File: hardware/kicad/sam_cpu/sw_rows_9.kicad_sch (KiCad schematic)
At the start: 47 parts, among them J12 J12 SWITCH ROWS, U10 LM339, U11 LM339, U18 74HC165

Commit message: Use 3.96 mm KK-396 footprints for the switch harness connectors
J1, J2, J3, J6, J12 and J13 are 0.156" headers on the original board, so
the existing harness plugs need KK-396, as already used for J10 and J11.

Co-Authored-By: Claude Opus 5.5 (1M context) <noreply@anthropic.com>
Claude-Session: https://claude.ai/code/session_019DLTv1F2PjepjxqiUcAMKV
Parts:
- J12: footprint Connector_Molex:Molex_KK-254_AE-6410-10A_1x10_P2.54mm_Vertical -> Connector_Molex:Molex_KK-396_A-41791-0010_1x10_P3.96mm_Vertical
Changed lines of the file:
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@@
 			)
 		)
-		(property "Footprint" "Connector_Molex:Molex_KK-254_AE-6410-10A_1x10_P2.54mm_Vertical"
+		(property "Footprint" "Connector_Molex:Molex_KK-396_A-41791-0010_1x10_P3.96mm_Vertical"
 			(at 20.32 147.32 0)
 			(hide yes)

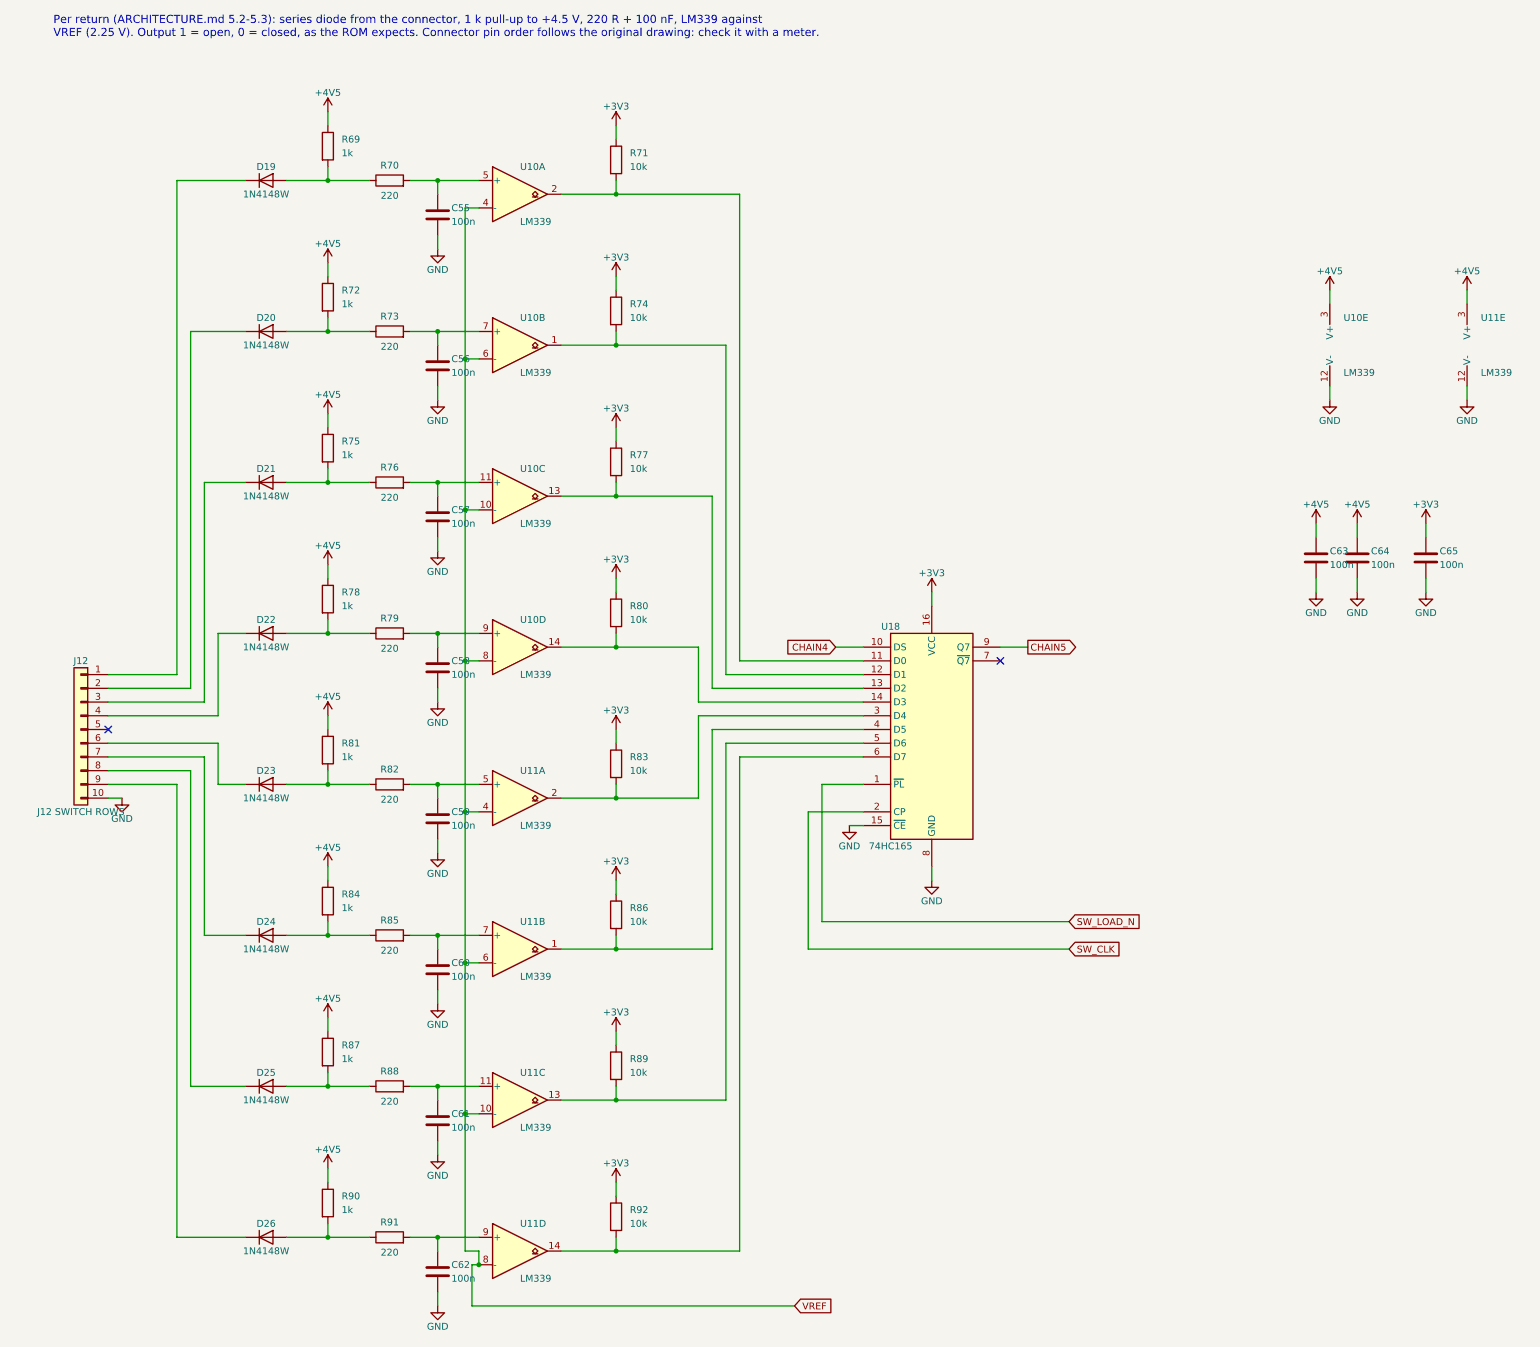
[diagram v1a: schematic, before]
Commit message: DIP switch block not loaded; larger schematic text
c30: SW3, R168-R175, U14 and C93 flagged DNP (schematic and board).
c31: schematic text 1.27 -> 1.6 mm (pins 1.5 mm), intersheet refs moved out.

Co-Authored-By: Claude Opus 5.5 (1M context) <noreply@anthropic.com>
Claude-Session: https://claude.ai/code/session_01ExuDVoDDDHhVWjb8EwVzYb
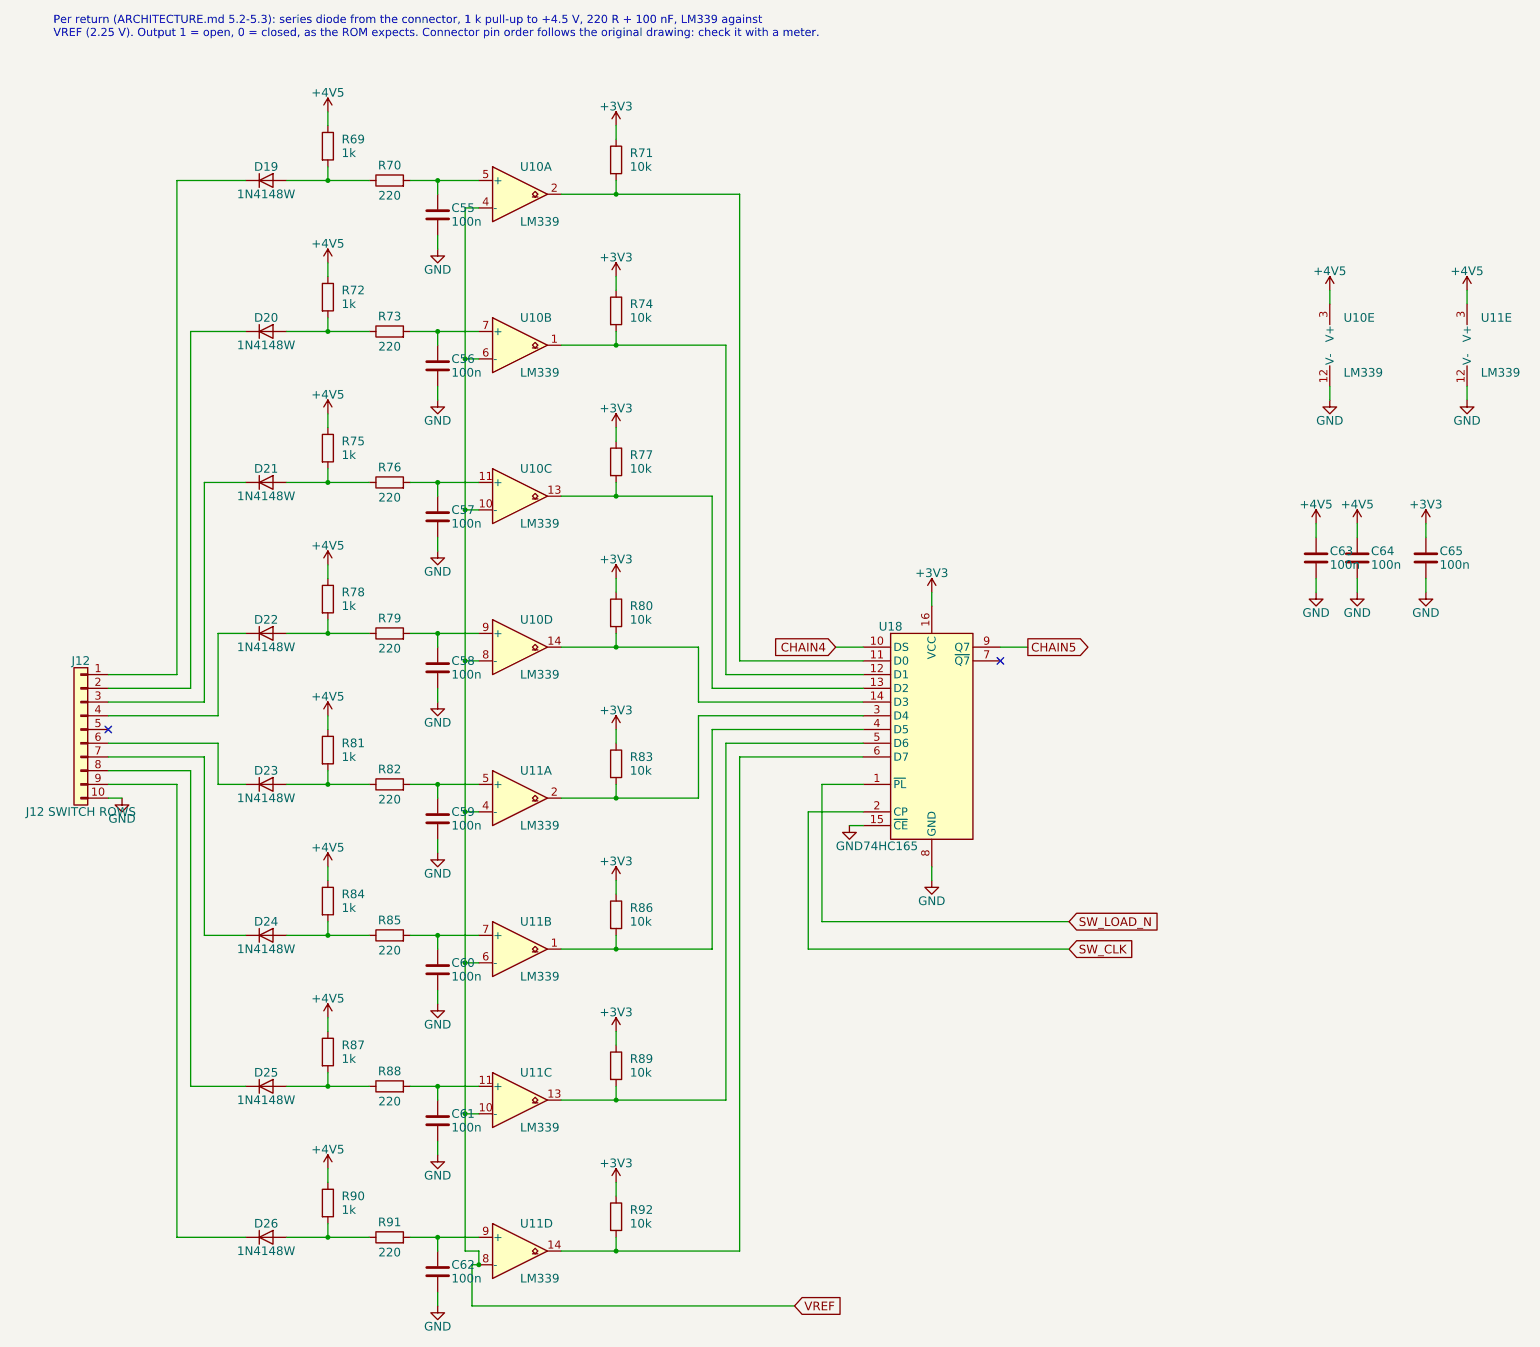
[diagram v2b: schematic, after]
